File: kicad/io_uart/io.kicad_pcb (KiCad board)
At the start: 2 copper layers, 160 x 100.3 mm, 72 parts, among them IC1 ATMEGA8-P, J1 DB9, P1 CONN_02X06, P2 SPI4, P3 ISP, P4 PS/2 Keyboard, P5 CONN_02X25, U1 G65SC22P, U10 16550, U11 MAX232, U2 DS1306, U3 7400, U4 74125, U5 LP2950, U6 7407, U7 LTV846, U8 LTV846, U9 74LS06, X1 CRYSTAL_SMD, X2 OSC

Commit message: xmodem
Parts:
- removed D1, D10, D2, D3, D4, D5, D6, D7, D8, D9: DIODE, Discret:D3
- removed U8: LTV846, Housings_DIP:DIP-16_W7.62mm_LongPads
- added R18: 1k, Discret:R3-LARGE_PADS, F.Cu at (208.3, 100.3)
- added R19: 1k, Discret:R3-LARGE_PADS, F.Cu at (205.7, 100.3)
- added R20: 1k, Discret:R3-LARGE_PADS, F.Cu at (134.6, 69.8)
- added R21: 1k, Discret:R3-LARGE_PADS, F.Cu at (134.6, 67.3)
- added RR1: 1k, Resistors_ThroughHole:Resistor_Array_SIP8, F.Cu at (152.4, 68.6)
- P1: value CONN_02X06 -> USERPORT; footprint Pin_Headers:Pin_Header_Straight_2x06 -> Pin_Headers:Pin_Header_Angled_2x06
- P2, P3: footprint Pin_Headers:Pin_Header_Straight_2x03 -> Pin_Headers:Pin_Header_Angled_2x03
- R1, R2, R3, R4, R5: footprint Discret:R3-LARGE_PADS -> Discret:R1
- R10, R11, R6, R7, R8, R9: value 12K-27K -> 1k
- R12, R13: value 220 -> 1k
- R14, R15: value 1K -> 1k
- U2: value DS1306 -> 7400; footprint Housings_DIP:DIP-16_W7.62mm_LongPads -> Housings_DIP:DIP-14_W7.62mm_LongPads
- U3: value 7400 -> 74LS244; footprint Housings_DIP:DIP-14_W7.62mm_LongPads -> Housings_DIP:DIP-20_W7.62mm_LongPads
- U7: value LTV846 -> DS1306
- moved P3 194.0 mm to (69.2, 68.6), turned to 180 degrees
- moved C1 183.1 mm to (81.3, 80.0), turned to 270 degrees
- moved C5 148.2 mm to (127.0, 78.7), turned to 270 degrees
- moved C12 147.9 mm to (104.1, 94.0)
- moved C3 128.5 mm to (128.3, 105.4), turned to 90 degrees
- moved P2 117.9 mm to (184.2, 58.4), turned to 90 degrees
- moved R8 108.1 mm to (191.8, 86.4), turned to 270 degrees
- moved R10 102.5 mm to (186.7, 86.4), turned to 270 degrees
- moved R7 101.0 mm to (194.3, 86.4), turned to 270 degrees
- moved X2 99.2 mm to (137.2, 125.7)
- moved R9 98.8 mm to (189.2, 86.4), turned to 270 degrees
- moved U10 98.4 mm to (199.4, 118.1), turned to 270 degrees
- moved C8 97.3 mm to (94.0, 77.5)
- moved R12 96.9 mm to (181.6, 86.4), turned to 270 degrees
- moved U7 94.4 mm to (108.0, 114.3), turned to 90 degrees
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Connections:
- IC1 pad 16: /~SPI_SS2 -> /PS/2 Controller/~SPI_SS
- IC1 pad 17: /SD Card/SPI_MOSI -> /PS/2 Controller/SPI_MOSI
- IC1 pad 18: Net-(IC1-Pad18) -> /PS/2 Controller/SPI_MISO
- IC1 pad 19: /SD Card/SPI_CLK -> /PS/2 Controller/SPI_CLK
- P1 pad 1: VCC -> /CA2
- P1 pad 10: /Joystick Ports/PortSel02 -> /Joystick Ports/J_Up
- P1 pad 11: /CA1 -> GND
- P1 pad 12: /CA2 -> VCC
- P1 pad 2: GND -> /CA1
- P1 pad 3: /Joystick Ports/J_Up -> /Joystick Ports/JOYPORT_SELECT
- P1 pad 4: /Joystick Ports/J_Down -> /PA6
- P1 pad 5: /Joystick Ports/J_Left -> /PA5
- P1 pad 6: /Joystick Ports/J_Right -> /Joystick Ports/J_Fire
- P1 pad 7: /Joystick Ports/J_Fire1 -> /Joystick Ports/J_Right
- P1 pad 8: /Joystick Ports/J_Fire2 -> /Joystick Ports/J_Left
- P1 pad 9: /Joystick Ports/PortSel01 -> /Joystick Ports/J_Down
- P2 pad 1: /SD Card/SPI_MISO -> /PS/2 Controller/SPI_MISO
- P2 pad 3: /SD Card/SPI_CLK -> /PS/2 Controller/SPI_CLK
- P2 pad 4: /SD Card/SPI_MOSI -> /PS/2 Controller/SPI_MOSI
- P3 pad 1: Net-(IC1-Pad18) -> /PS/2 Controller/SPI_MISO
- P3 pad 3: /SD Card/SPI_CLK -> /PS/2 Controller/SPI_CLK
- P3 pad 4: /SD Card/SPI_MOSI -> /PS/2 Controller/SPI_MOSI
- Port1 pad 1: Net-(D5-Pad2) -> Net-(Port1-Pad1)
- Port1 pad 2: Net-(D3-Pad2) -> Net-(Port1-Pad2)
- Port1 pad 3: Net-(D2-Pad2) -> Net-(Port1-Pad3)
- Port1 pad 4: Net-(D1-Pad2) -> Net-(Port1-Pad4)
- Port1 pad 6: Net-(D4-Pad2) -> Net-(Port1-Pad6)
- Port1 pad 8: Net-(Port1-Pad8) -> GND
- Port2 pad 1: Net-(D10-Pad2) -> Net-(Port2-Pad1)
- Port2 pad 2: Net-(D8-Pad2) -> Net-(Port2-Pad2)
- Port2 pad 3: Net-(D7-Pad2) -> Net-(Port2-Pad3)
- Port2 pad 4: Net-(D6-Pad2) -> Net-(Port2-Pad4)
- Port2 pad 6: Net-(D9-Pad2) -> Net-(Port2-Pad6)
- Port2 pad 8: Net-(Port2-Pad8) -> GND
- R10 pad 1: VCC -> /Joystick Ports/J_Fire
- R10 pad 2: /Joystick Ports/J_Right -> Net-(R10-Pad2)
- R11 pad 1: VCC -> /PA5
- R11 pad 2: /Joystick Ports/J_Left -> Net-(R11-Pad2)
- R12 pad 1: GND -> /PA6
- R13 pad 1: GND -> /Joystick Ports/JOYPORT_SELECT
- R14 pad 1: VCC -> /SD Card/SD_WRITE_PROTECT
- R15 pad 1: VCC -> /SD Card/SD_CARD_DETECT
- R6 pad 1: VCC -> /Joystick Ports/J_Up
- R6 pad 2: /Joystick Ports/J_Fire2 -> Net-(R6-Pad2)
- R7 pad 1: VCC -> /Joystick Ports/J_Down
- R7 pad 2: /Joystick Ports/J_Fire1 -> Net-(R7-Pad2)
- R8 pad 1: VCC -> /Joystick Ports/J_Left
- R8 pad 2: /Joystick Ports/J_Down -> Net-(R8-Pad2)
- R9 pad 1: VCC -> /Joystick Ports/J_Right
- R9 pad 2: /Joystick Ports/J_Up -> Net-(R9-Pad2)
- U1 pad 10: /SD Card/SPI_CLK -> /PS/2 Controller/SPI_CLK
- U1 pad 12: /~SPI_SS2 -> /PS/2 Controller/~SPI_SS
- U1 pad 13: /~SPI_SS3 -> /RTC/SPI_SS
- U1 pad 15: /SD Card/SD_WRITE_PROTECT -> Net-(R14-Pad2)
- U1 pad 16: /SD Card/SD_CARD_DETECT -> Net-(R15-Pad2)
- U1 pad 17: /SD Card/SPI_MOSI -> /PS/2 Controller/SPI_MOSI
- U1 pad 18: /SD Card/SPI_CLK -> /PS/2 Controller/SPI_CLK
- U1 pad 19: /SD Card/SPI_MISO -> /PS/2 Controller/SPI_MISO
- U1 pad 2: /Joystick Ports/J_Up -> Net-(R6-Pad2)
- U1 pad 3: /Joystick Ports/J_Down -> Net-(R7-Pad2)
- U1 pad 39: /CA2 -> Net-(R19-Pad2)
- U1 pad 4: /Joystick Ports/J_Left -> Net-(R8-Pad2)
- U1 pad 40: /CA1 -> Net-(R18-Pad2)
- U1 pad 5: /Joystick Ports/J_Right -> Net-(R9-Pad2)
- U1 pad 6: /Joystick Ports/J_Fire1 -> Net-(R10-Pad2)
- U1 pad 7: /Joystick Ports/J_Fire2 -> Net-(R11-Pad2)
- U1 pad 8: /Joystick Ports/PortSel01 -> Net-(R12-Pad2)
- U1 pad 9: /Joystick Ports/PortSel02 -> Net-(R13-Pad2)
- U10 pad 34: Net-(U10-Pad34) -> /Joystick Ports//JOYPORT_ENABLE
- U2 pad 1: GND -> /Joystick Ports/JOYPORT_SELECT
- U2 pad 11: /SD Card/SPI_CLK -> Net-(U2-Pad11)
- U2 pad 12: /SD Card/SPI_MOSI -> /RTC/SPI_SS
- U2 pad 13: Net-(U2-Pad13) -> /RTC/SPI_SS
- U2 pad 2: Net-(BT1-Pad1) -> /Joystick Ports/JOYPORT_SELECT
- U2 pad 3: Net-(U2-Pad3) -> Net-(U2-Pad10)
- U2 pad 4: Net-(U2-Pad4) -> /Joystick Ports/JOYPORT_SELECT
- U2 pad 5: /IRQ -> /Joystick Ports//JOYPORT_ENABLE
- U2 pad 7: Net-(U2-Pad7) -> GND
- U2 pad 8: GND -> Net-(U2-Pad8)
- U2 pad 9: VCC -> /Joystick Ports//JOYPORT_ENABLE
- U3 pad 1: /~SPI_SS3 -> Net-(U2-Pad8)
- U3 pad 10: /Joystick Ports/PortSel02 -> GND
- U3 pad 11: (no net) -> Net-(Port1-Pad1)
- U3 pad 12: (no net) -> /Joystick Ports/J_Right
- U3 pad 13: (no net) -> Net-(Port1-Pad2)
- U3 pad 14: VCC -> /Joystick Ports/J_Left
- U3 pad 2: /~SPI_SS3 -> Net-(Port2-Pad1)
- U3 pad 3: Net-(U2-Pad10) -> /Joystick Ports/J_Right
- U3 pad 4: /Joystick Ports/PortSel01 -> Net-(Port2-Pad2)
- U3 pad 5: /Joystick Ports/PortSel01 -> /Joystick Ports/J_Left
- U3 pad 6: Net-(U3-Pad6) -> Net-(Port2-Pad3)
- U3 pad 7: GND -> /Joystick Ports/J_Down
- U3 pad 8: Net-(U3-Pad8) -> Net-(Port2-Pad4)
- U3 pad 9: /Joystick Ports/PortSel02 -> /Joystick Ports/J_Up
- U4 pad 1: /~SPI_SS3 -> Net-(U2-Pad6)
- U4 pad 2: Net-(U2-Pad13) -> Net-(Port1-Pad6)
- U4 pad 3: /SD Card/SPI_MISO -> /Joystick Ports/J_Fire
- U4 pad 4: /~SPI_SS2 -> Net-(U2-Pad8)
- U4 pad 5: Net-(IC1-Pad18) -> Net-(Port2-Pad6)
- U4 pad 6: /SD Card/SPI_MISO -> /Joystick Ports/J_Fire
- U4 pad 8: /SD Card/SPI_MISO -> /PS/2 Controller/SPI_MISO
- U6 pad 1: /SD Card/SPI_SS1 -> (no net)
- U6 pad 10: (no net) -> Net-(R2-Pad2)
- U6 pad 11: (no net) -> /PS/2 Controller/SPI_MOSI
- U6 pad 12: (no net) -> Net-(R3-Pad2)
- U6 pad 13: (no net) -> /SD Card/SPI_SS1
- U6 pad 2: Net-(R3-Pad2) -> (no net)
- U6 pad 3: /SD Card/SPI_MOSI -> (no net)
- U6 pad 4: Net-(R2-Pad2) -> (no net)
- U6 pad 5: /SD Card/SPI_CLK -> (no net)
- U6 pad 6: Net-(R1-Pad2) -> (no net)
- U6 pad 8: (no net) -> Net-(R1-Pad2)
- U6 pad 9: (no net) -> /PS/2 Controller/SPI_CLK
- U7 pad 1: Net-(R14-Pad2) -> GND
- U7 pad 10: /Joystick Ports/J_Right -> Net-(U2-Pad11)
- U7 pad 11: GND -> /PS/2 Controller/SPI_CLK
- U7 pad 12: /Joystick Ports/J_Left -> /PS/2 Controller/SPI_MOSI
- U7 pad 13: Net-(R13-Pad2) -> /PS/2 Controller/SPI_MISO
- U7 pad 14: Net-(Port2-Pad8) -> VCC
- U7 pad 15: Net-(R12-Pad2) -> Net-(U7-Pad15)
- U7 pad 16: Net-(Port1-Pad8) -> VCC
- U7 pad 2: Net-(U3-Pad6) -> Net-(BT1-Pad1)
- U7 pad 3: Net-(R15-Pad2) -> Net-(U7-Pad3)
- U7 pad 4: Net-(U3-Pad8) -> Net-(U7-Pad4)
- U7 pad 5: VCC -> /IRQ
- U7 pad 7: VCC -> Net-(U7-Pad7)
- U7 pad 8: Net-(D1-Pad1) -> GND
- U7 pad 9: GND -> VCC
- X1 pad 1: Net-(U2-Pad4) -> Net-(U7-Pad4)
- X1 pad 2: Net-(U2-Pad3) -> Net-(U7-Pad3)
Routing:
- net GND: track 193.7 -> 471.0 mm
- net /RESET: track 0.00 -> 237.9 mm, vias 0 -> 6
- net /IRQ: track 0.00 -> 196.0 mm, vias 0 -> 3
- net /PS/2 Controller/SPI_CLK: track 0.00 -> 192.7 mm
- net /Connector/RESET_TRIG: track 0.00 -> 191.7 mm, vias 0 -> 3
- net /PS/2 Controller/SPI_MOSI: track 0.00 -> 182.5 mm, vias 0 -> 3
- net /PS/2 Controller/SPI_MISO: track 0.00 -> 176.6 mm
- net /NMI: track 0.00 -> 170.6 mm, vias 0 -> 1
- net VCC: track 149.2 -> 306.3 mm
- net /Joystick Ports/JOYPORT_SELECT: track 0.00 -> 122.5 mm, vias 0 -> 2
- net Net-(U10-Pad36): track 0.00 -> 113.3 mm
- net /Joystick Ports//JOYPORT_ENABLE: track 0.00 -> 105.9 mm, vias 0 -> 1
- net Net-(U10-Pad32): track 0.00 -> 100.0 mm
- net /Connector/D7: track 0.00 -> 98.0 mm
- net /Joystick Ports/J_Fire: track 0.00 -> 97.7 mm, vias 0 -> 2
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- added copper zone on F.Cu, net GND

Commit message: 244 wiring
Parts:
- moved U3 7.62 mm to (130.8, 87.6)
- moved R20 5.08 mm to (129.5, 69.8)
- moved R21 5.08 mm to (129.5, 67.3)
- moved C5 1.18 mm to (127.0, 79.9)
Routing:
- net Net-(Port2-Pad4): track 0.00 -> 51.5 mm
- net Net-(Port2-Pad3): track 0.00 -> 46.3 mm
- net Net-(Port2-Pad2): track 0.00 -> 43.9 mm
- net VCC: track 306.3 -> 342.1 mm
- net /Joystick Ports/J_Up: track 31.9 -> 60.5 mm, vias 0 -> 2
- net Net-(Port2-Pad1): track 0.00 -> 27.7 mm
- net Net-(Port1-Pad4): track 0.00 -> 26.3 mm
- net GND: track 471.0 -> 496.7 mm, vias 0 -> 2
- net Net-(Port1-Pad3): track 0.00 -> 25.4 mm
- net Net-(Port1-Pad2): track 0.00 -> 24.6 mm
- net /Joystick Ports/J_Right: track 30.4 -> 53.3 mm, vias 0 -> 2
- net /Joystick Ports/J_Down: track 29.4 -> 45.8 mm, vias 0 -> 2
- net Net-(Port1-Pad1): track 0.00 -> 14.1 mm
- net Net-(Port1-Pad6): track 0.00 -> 12.1 mm
- net /Joystick Ports/J_Left: track 33.0 -> 42.9 mm
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
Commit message: io board release candidate
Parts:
- C1, C10, C2, C3, C5, C7, C9: footprint Capacitors_ThroughHole:C_Rect_L4_W2.5_P2.5 -> Capacitors_ThroughHole:C_Disc_D3_P2.5
- C4: footprint Capacitors_ThroughHole:C_Radial_D8_L11.5_P3.5 -> Capacitors_ThroughHole:C_Disc_D3_P2.5
- C6: footprint Capacitors_ThroughHole:C_Radial_D6.3_L11.2_P2.5 -> Capacitors_ThroughHole:C_Radial_D5_L6_P2.5
- C8: footprint Capacitors_ThroughHole:C_Rect_L4_W2.5_P2.5 -> Capacitors_ThroughHole:C_Radial_D8_L11.5_P3.5
- P1: footprint Pin_Headers:Pin_Header_Angled_2x06 -> Pin_Headers:Pin_Header_Angled_2x08
- R1, R2, R3, R4, R5: footprint Discret:R1 -> Resistors_ThroughHole:Resistor_Horizontal_RM7mm
- R10, R11, R12, R13, R14, R15, R16, R17, R18, R19, R20, R21, R6, R7, R8, R9: footprint Discret:R3-LARGE_PADS -> Resistors_ThroughHole:Resistor_Horizontal_RM7mm
- U5: footprint TO_SOT_Packages_THT:TO-92_Inline_Wide -> TO_SOT_Packages_THT:TO-92_Inline_Narrow_Oval
- moved C11 102.0 mm to (205.7, 115.6), turned to 90 degrees
- moved C4 91.5 mm to (129.5, 95.2)
- moved C12 83.0 mm to (182.8, 120.7)
- moved R18 80.7 mm to (137.2, 62.2)
- moved R19 75.1 mm to (141.0, 62.2)
- moved P1 73.7 mm to (123.2, 58.4)
- moved P2 69.9 mm to (114.3, 58.4)
- moved C1 69.8 mm to (151.1, 80.0), turned to 180 degrees
- moved Port2 66.0 mm to (193.0, 61.0)
- moved U9 57.6 mm to (186.7, 128.3)
- moved C17 51.8 mm to (135.9, 134.6), turned to 0 degrees
- moved U11 50.6 mm to (130.8, 129.5)
- moved C2 50.2 mm to (104.1, 108.0), turned to 270 degrees
- moved C16 49.4 mm to (135.9, 139.7), turned to 0 degrees
- moved C15 48.6 mm to (130.8, 134.6), turned to 0 degrees
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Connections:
- P1 pad 1: /CA2 -> /Joystick Ports/J_Up
- P1 pad 10: /Joystick Ports/J_Up -> VCC
- P1 pad 11: GND -> Net-(P1-Pad11)
- P1 pad 12: VCC -> Net-(P1-Pad12)
- P1 pad 2: /CA1 -> /Joystick Ports/J_Down
- P1 pad 3: /Joystick Ports/JOYPORT_SELECT -> /Joystick Ports/J_Left
- P1 pad 4: /PA6 -> /Joystick Ports/J_Right
- P1 pad 5: /PA5 -> /Joystick Ports/J_Fire
- P1 pad 6: /Joystick Ports/J_Fire -> /PA5
- P1 pad 7: /Joystick Ports/J_Right -> /PA6
- P1 pad 8: /Joystick Ports/J_Left -> /Joystick Ports/JOYPORT_SELECT
- P1 pad 9: /Joystick Ports/J_Down -> GND
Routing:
- net GND: track 496.7 -> 672.8 mm, vias 2 -> 4
- net Net-(Port2-Pad6): track 8.51 -> 141.0 mm, vias 0 -> 4
- net VCC: track 342.1 -> 466.0 mm, vias 0 -> 6
- net Net-(Port2-Pad1): track 27.7 -> 111.4 mm, vias 0 -> 3
- net Net-(R18-Pad2): track 11.1 -> 92.1 mm, vias 0 -> 4
- net /IRQ: track 196.0 -> 276.8 mm, vias 3 -> 8
- net /Joystick Ports/J_Down: track 45.8 -> 121.8 mm, vias 2 -> 5
- net /RESET: track 237.9 -> 312.6 mm, vias 6 -> 8
- net Net-(R19-Pad2): track 11.2 -> 83.2 mm, vias 0 -> 3
- net /Joystick Ports/J_Right: track 53.3 -> 123.8 mm, vias 2 -> 5
- net /Joystick Ports/J_Left: track 42.9 -> 113.0 mm, vias 0 -> 5
- net /Joystick Ports/J_Up: track 60.5 -> 129.7 mm, vias 2 -> 3
- net Net-(Port2-Pad2): track 43.9 -> 109.6 mm, vias 0 -> 4
- net Net-(Port1-Pad6): track 12.1 -> 77.3 mm, vias 0 -> 2
- net Net-(J1-Pad8): track 23.0 -> 81.7 mm
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
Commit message: cosmetics
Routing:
- net Net-(Port1-Pad2): track 39.9 -> 38.0 mm
- net GND: track 672.8 -> 674.2 mm
- net /Joystick Ports/JOYPORT_SELECT: track 138.2 -> 137.0 mm
- net Net-(R19-Pad2): track 83.2 -> 84.2 mm
- net /Joystick Ports/J_Up: track 129.7 -> 130.6 mm
- net Net-(R15-Pad2): track 79.4 -> 78.5 mm
- net Net-(Port2-Pad1): track 111.4 -> 110.6 mm
- net /Joystick Ports/J_Down: track 121.8 -> 122.4 mm
- net Net-(Port1-Pad3): track 42.6 -> 43.2 mm
- net /PA6: track 71.2 -> 71.7 mm

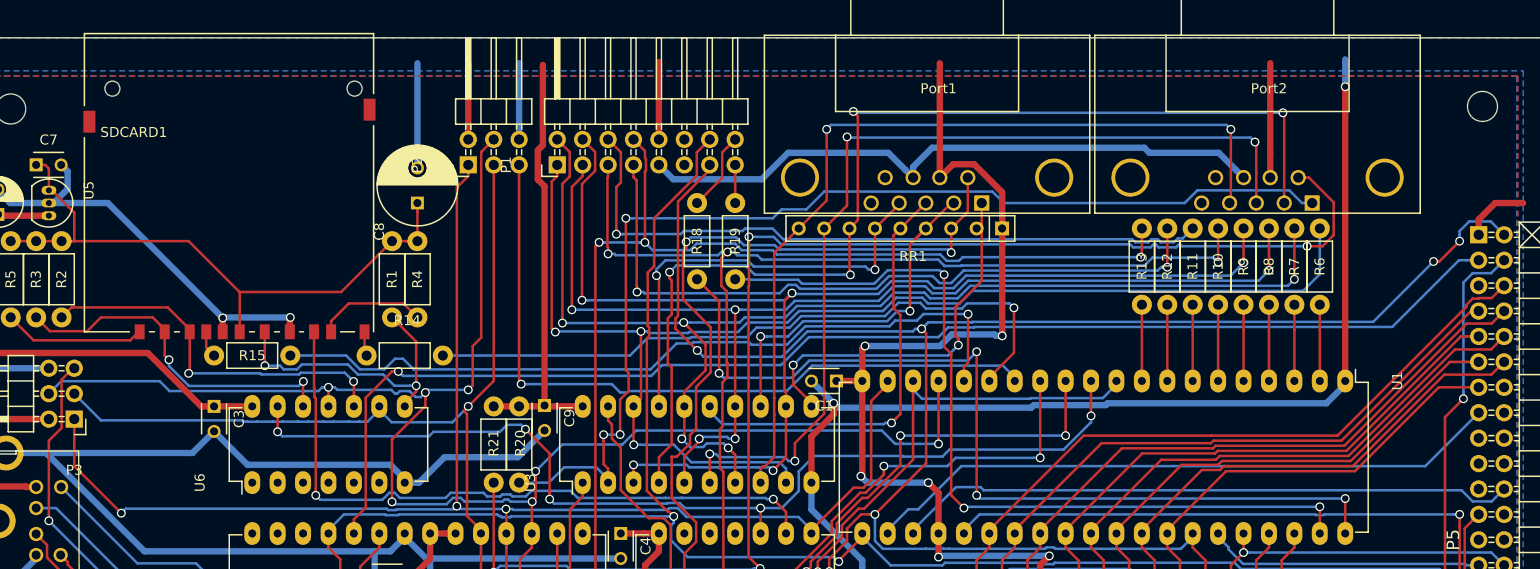
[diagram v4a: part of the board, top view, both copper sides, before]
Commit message: C8 fix footprint
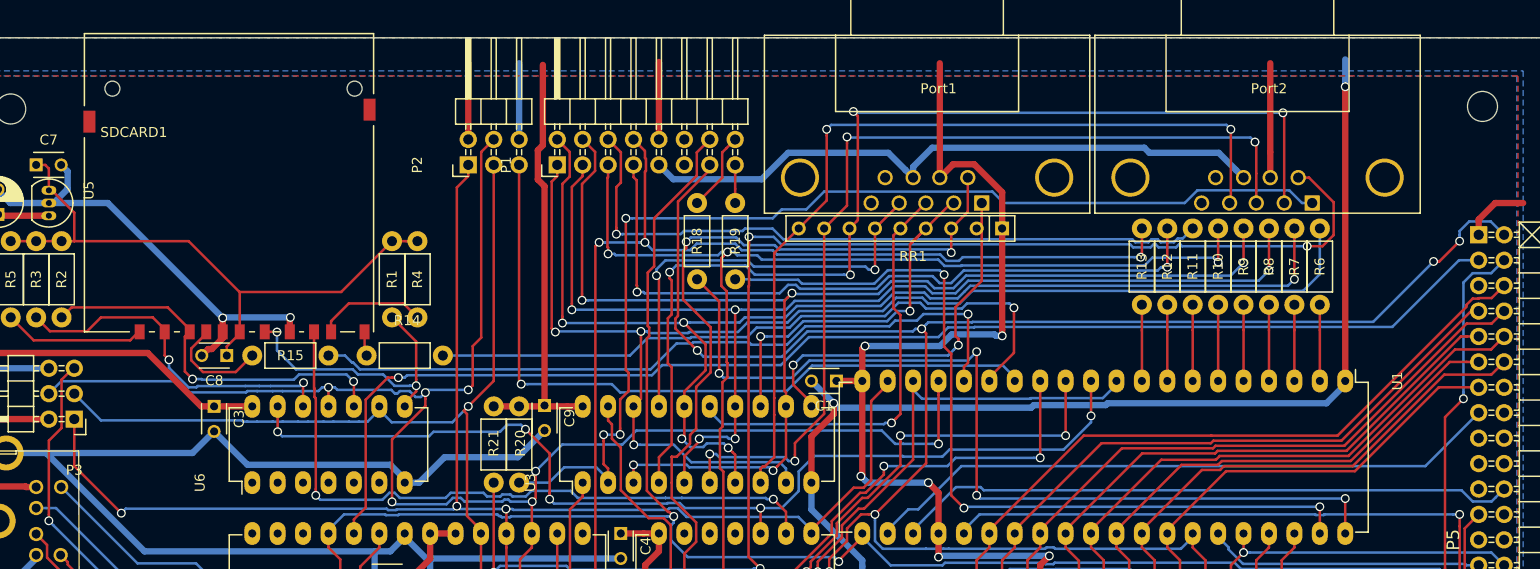
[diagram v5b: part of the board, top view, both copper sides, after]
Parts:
- C8: footprint Capacitors_ThroughHole:C_Radial_D8_L11.5_P3.5 -> Capacitors_ThroughHole:C_Disc_D3_P2.5
- moved C8 24.4 mm to (90.2, 77.5), turned to 180 degrees
- moved R15 3.81 mm to (92.7, 77.5)
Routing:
- net /SD Card/SD_CARD_DETECT: track 2.70 -> 10.7 mm
- net GND: track 674.2 -> 667.1 mm
- net Net-(R15-Pad2): track 78.5 -> 73.8 mm
- net Net-(R1-Pad2): track 30.1 -> 28.8 mm
- net Net-(C7-Pad1): track 62.6 -> 61.7 mm
- net Net-(R2-Pad2): track 38.4 -> 39.1 mm

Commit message: trace cosmetics
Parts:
- moved P2 3.81 mm to (110.5, 58.4)
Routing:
- net /PS/2 Controller/SPI_MOSI: track 168.3 -> 158.0 mm, vias 7 -> 6
- net /~SPI_SS4: track 73.6 -> 77.4 mm
- net /PS/2 Controller/SPI_CLK: track 175.4 -> 173.3 mm
- net Net-(R1-Pad2): track 28.8 -> 27.7 mm
- net /SD Card/SPI_SS1: track 102.1 -> 101.1 mm
- net Net-(R15-Pad2): track 73.8 -> 74.4 mm

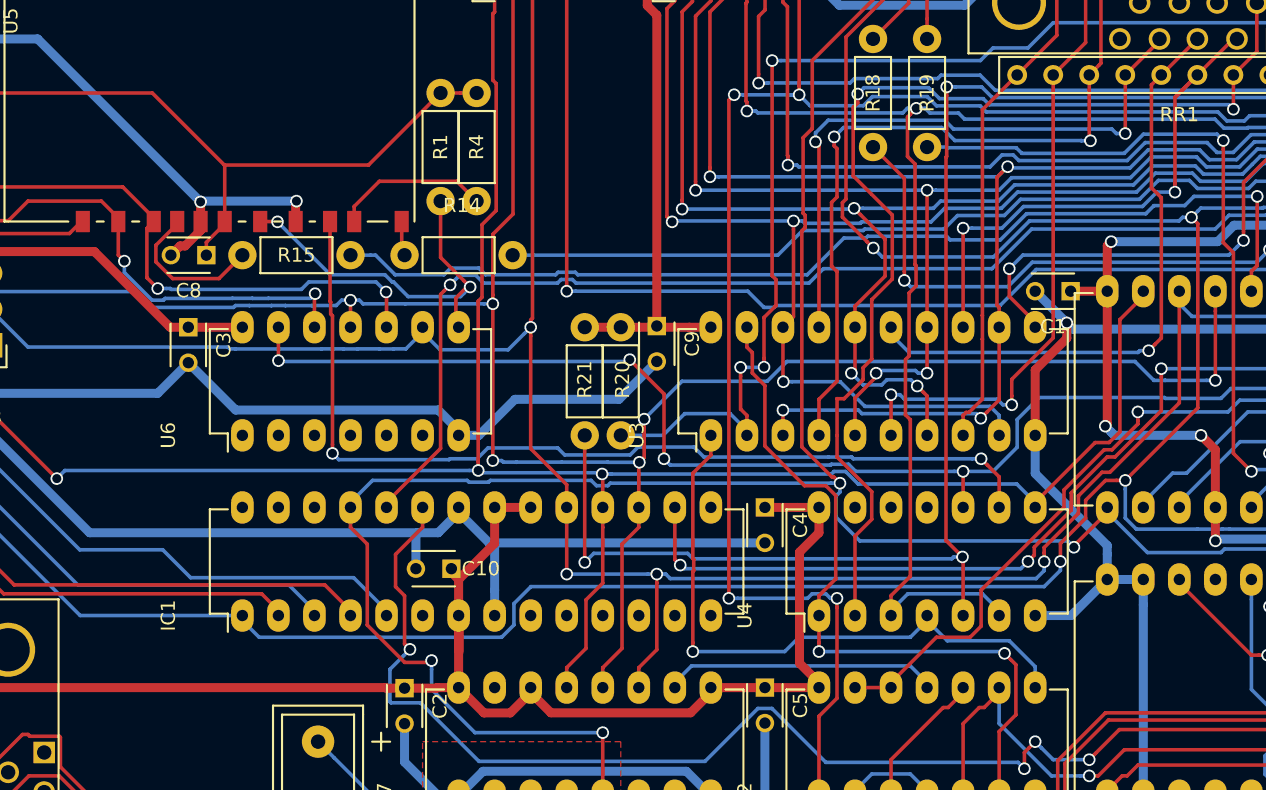
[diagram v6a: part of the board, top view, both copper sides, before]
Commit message: moved C10 a bit, cosmetics
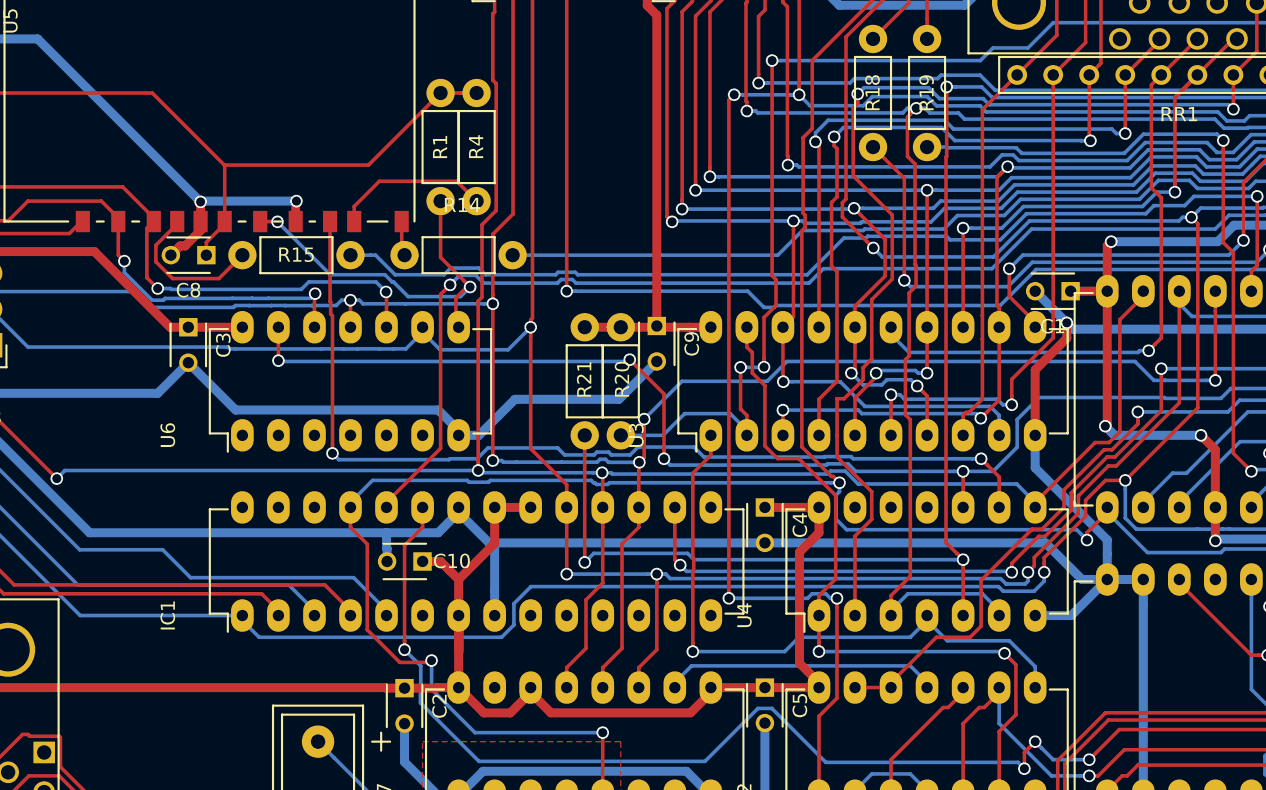
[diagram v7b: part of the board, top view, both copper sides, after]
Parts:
- moved C10 2.09 mm to (105.4, 99.1)
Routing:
- net GND: track 667.3 -> 691.9 mm
- net /Connector/RESET_TRIG: track 139.5 -> 136.7 mm
- net VCC: track 466.0 -> 468.1 mm

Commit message: cleanup
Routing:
- net Net-(Port2-Pad2): track 109.6 -> 102.0 mm
- net Net-(Port2-Pad4): track 86.3 -> 81.9 mm
- net Net-(R14-Pad2): track 68.2 -> 64.9 mm
- net Net-(Port2-Pad3): track 93.3 -> 90.0 mm
- net Net-(Port1-Pad6): track 76.9 -> 78.4 mm
- net Net-(R19-Pad2): track 84.2 -> 85.0 mm
